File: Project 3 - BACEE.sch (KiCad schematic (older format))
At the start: 12 parts

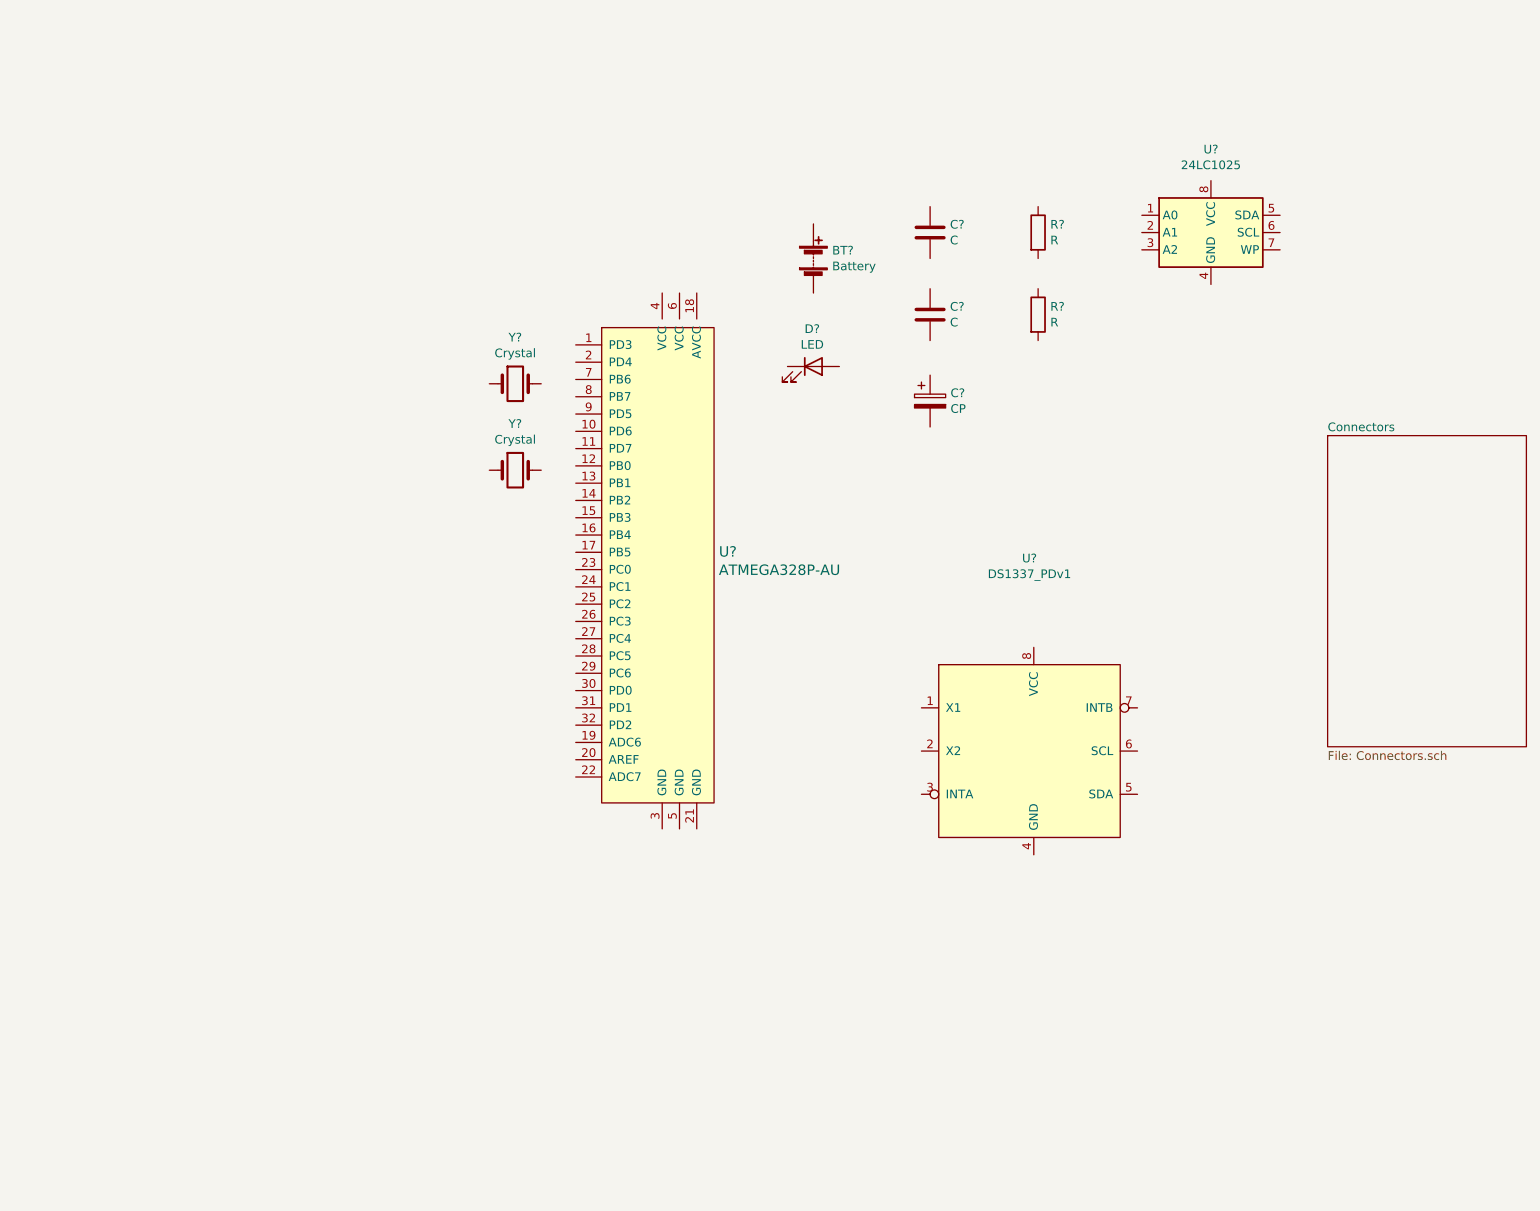
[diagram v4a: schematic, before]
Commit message: Arrenged symbols.
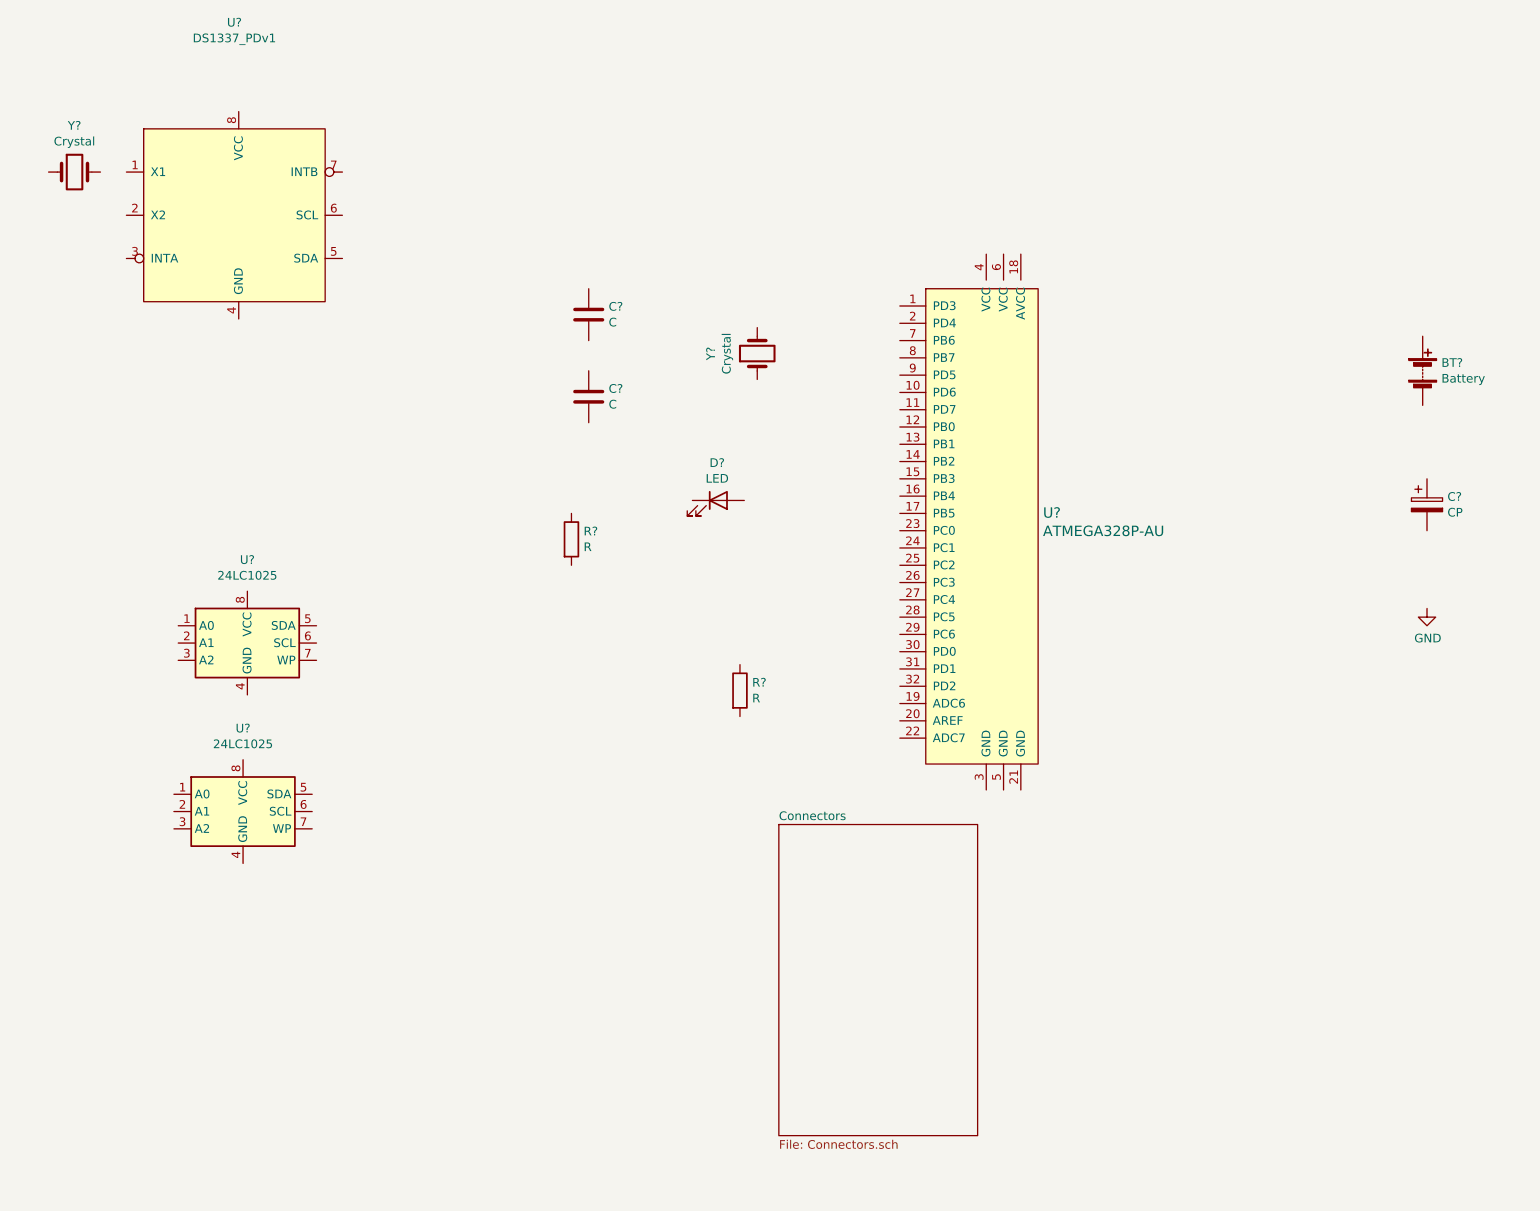
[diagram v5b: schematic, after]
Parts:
- added U?: 24LC1025, symbol Memory_EEPROM:24LC1025
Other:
- moved on the sheet: BT?, C?, D?, R?, U?, Y?
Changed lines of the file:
@@
 L Device:Battery BT?
 U 1 1 5F0CDB03
-P 5375 2275
-F 0 "BT?" H 5483 2321 50  0000 L CNN
-F 1 "Battery" H 5483 2230 50  0000 L CNN
-F 2 "" V 5375 2335 50  0001 C CNN
-F 3 "~" V 5375 2335 50  0001 C CNN
-	1    5375 2275
+P 8900 2925
+F 0 "BT?" H 9008 2971 50  0000 L CNN
+F 1 "Battery" H 9008 2880 50  0000 L CNN
+F 2 "" V 8900 2985 50  0001 C CNN
+F 3 "~" V 8900 2985 50  0001 C CNN
+	1    8900 2925
 	1    0    0    -1
 $EndComp
@@
 L Device:C C?
 U 1 1 5F0CEA38
-P 6050 2125
-F 0 "C?" H 6165 2171 50  0000 L CNN
-F 1 "C" H 6165 2080 50  0000 L CNN
-F 2 "" H 6088 1975 50  0001 C CNN
-F 3 "~" H 6050 2125 50  0001 C CNN
-	1    6050 2125
+P 4075 2600
+F 0 "C?" H 4190 2646 50  0000 L CNN
+F 1 "C" H 4190 2555 50  0000 L CNN
+F 2 "" H 4113 2450 50  0001 C CNN
+F 3 "~" H 4075 2600 50  0001 C CNN
+	1    4075 2600
 	1    0    0    -1
 $EndComp
@@
 L Device:C C?
 U 1 1 5F0CF2D4
-P 6050 2600
-F 0 "C?" H 6165 2646 50  0000 L CNN
-F 1 "C" H 6165 2555 50  0000 L CNN
-F 2 "" H 6088 2450 50  0001 C CNN
-F 3 "~" H 6050 2600 50  0001 C CNN
-	1    6050 2600
+P 4075 3075
+F 0 "C?" H 4190 3121 50  0000 L CNN
+F 1 "C" H 4190 3030 50  0000 L CNN
+F 2 "" H 4113 2925 50  0001 C CNN
+F 3 "~" H 4075 3075 50  0001 C CNN
+	1    4075 3075
 	1    0    0    -1
 $EndComp
@@
 L Device:CP C?
 U 1 1 5F0CF8DC
-P 6050 3100
-F 0 "C?" H 6168 3146 50  0000 L CNN
-F 1 "CP" H 6168 3055 50  0000 L CNN
-F 2 "" H 6088 2950 50  0001 C CNN
-F 3 "~" H 6050 3100 50  0001 C CNN
-	1    6050 3100
+P 8925 3700
+F 0 "C?" H 9043 3746 50  0000 L CNN
+F 1 "CP" H 9043 3655 50  0000 L CNN
+F 2 "" H 8963 3550 50  0001 C CNN
+F 3 "~" H 8925 3700 50  0001 C CNN
+	1    8925 3700
 	1    0    0    -1
 $EndComp
@@
 L Device:LED D?
 U 1 1 5F0CFE76
-P 5375 2900
-F 0 "D?" H 5368 3117 50  0000 C CNN
-F 1 "LED" H 5368 3026 50  0000 C CNN
-F 2 "" H 5375 2900 50  0001 C CNN
-F 3 "~" H 5375 2900 50  0001 C CNN
-	1    5375 2900
+P 4825 3675
+F 0 "D?" H 4818 3892 50  0000 C CNN
+F 1 "LED" H 4818 3801 50  0000 C CNN
+F 2 "" H 4825 3675 50  0001 C CNN
+F 3 "~" H 4825 3675 50  0001 C CNN
+	1    4825 3675
 	1    0    0    -1
 $EndComp
@@
 L Device:R R?
 U 1 1 5F0D09EF
-P 6675 2125
-F 0 "R?" H 6745 2171 50  0000 L CNN
-F 1 "R" H 6745 2080 50  0000 L CNN
-F 2 "" V 6605 2125 50  0001 C CNN
-F 3 "~" H 6675 2125 50  0001 C CNN
-	1    6675 2125
+P 3975 3900
+F 0 "R?" H 4045 3946 50  0000 L CNN
+F 1 "R" H 4045 3855 50  0000 L CNN
+F 2 "" V 3905 3900 50  0001 C CNN
+F 3 "~" H 3975 3900 50  0001 C CNN
+	1    3975 3900
 	1    0    0    -1
 $EndComp
@@
 L Device:R R?
 U 1 1 5F0D11B8
-P 6675 2600
-F 0 "R?" H 6745 2646 50  0000 L CNN
-F 1 "R" H 6745 2555 50  0000 L CNN
-F 2 "" V 6605 2600 50  0001 C CNN
-F 3 "~" H 6675 2600 50  0001 C CNN
-	1    6675 2600
+P 4950 4775
+F 0 "R?" H 5020 4821 50  0000 L CNN
+F 1 "R" H 5020 4730 50  0000 L CNN
+F 2 "" V 4880 4775 50  0001 C CNN
+F 3 "~" H 4950 4775 50  0001 C CNN
+	1    4950 4775
 	1    0    0    -1
 $EndComp
@@
 L Memory_EEPROM:24LC1025 U?
 U 1 1 5F0D1B59
-P 7675 2125
-F 0 "U?" H 7675 2606 50  0000 C CNN
-F 1 "24LC1025" H 7675 2515 50  0000 C CNN
-F 2 "" H 7675 2125 50  0001 C CNN
-F 3 "http://ww1.microchip.com/downloads/en/DeviceDoc/21941B.pdf" H 7675 2125 50  0001 C CNN
-	1    7675 2125
+P 2100 4500
+F 0 "U?" H 2100 4981 50  0000 C CNN
+F 1 "24LC1025" H 2100 4890 50  0000 C CNN
+F 2 "" H 2100 4500 50  0001 C CNN
+F 3 "http://ww1.microchip.com/downloads/en/DeviceDoc/21941B.pdf" H 2100 4500 50  0001 C CNN
+	1    2100 4500
 	1    0    0    -1
 $EndComp
 $Sheet
-S 8350 3300 1150 1800
+S 5175 5550 1150 1800
 U 5F0D3531
 F0 "Connectors" 50
@@
 L dk_Embedded-Microcontrollers:ATMEGA328P-AU U?
 U 1 1 5F0D825C
-P 4500 4075
-F 0 "U?" H 4828 4178 60  0000 L CNN
-F 1 "ATMEGA328P-AU" H 4828 4072 60  0000 L CNN
-F 2 "digikey-footprints:TQFP-32_7x7mm" H 4700 4275 60  0001 L CNN
-F 3 "http://www.microchip.com/mymicrochip/filehandler.aspx?ddocname=en608326" H 4700 4375 60  0001 L CNN
-F 4 "ATMEGA328P-AU-ND" H 4700 4475 60  0001 L CNN "Digi-Key_PN"
-F 5 "ATMEGA328P-AU" H 4700 4575 60  0001 L CNN "MPN"
-F 6 "Integrated Circuits (ICs)" H 4700 4675 60  0001 L CNN "Category"
-F 7 "Embedded - Microcontrollers" H 4700 4775 60  0001 L CNN "Family"
-F 8 "http://www.microchip.com/mymicrochip/filehandler.aspx?ddocname=en608326" H 4700 4875 60  0001 L CNN "DK_Datasheet_Link"
-F 9 "/product-detail/en/microchip-technology/ATMEGA328P-AU/ATMEGA328P-AU-ND/1832260" H 4700 4975 60  0001 L CNN "DK_Detail_Page"
-F 10 "IC MCU 8BIT 32KB FLASH 32TQFP" H 4700 5075 60  0001 L CNN "Description"
-F 11 "Microchip Technology" H 4700 5175 60  0001 L CNN "Manufacturer"
-F 12 "Active" H 4700 5275 60  0001 L CNN "Status"
-	1    4500 4075
+P 6375 3850
+F 0 "U?" H 6703 3953 60  0000 L CNN
+F 1 "ATMEGA328P-AU" H 6703 3847 60  0000 L CNN
+F 2 "digikey-footprints:TQFP-32_7x7mm" H 6575 4050 60  0001 L CNN
+F 3 "http://www.microchip.com/mymicrochip/filehandler.aspx?ddocname=en608326" H 6575 4150 60  0001 L CNN
+F 4 "ATMEGA328P-AU-ND" H 6575 4250 60  0001 L CNN "Digi-Key_PN"
+F 5 "ATMEGA328P-AU" H 6575 4350 60  0001 L CNN "MPN"
+F 6 "Integrated Circuits (ICs)" H 6575 4450 60  0001 L CNN "Category"
+F 7 "Embedded - Microcontrollers" H 6575 4550 60  0001 L CNN "Family"
+F 8 "http://www.microchip.com/mymicrochip/filehandler.aspx?ddocname=en608326" H 6575 4650 60  0001 L CNN "DK_Datasheet_Link"
+F 9 "/product-detail/en/microchip-technology/ATMEGA328P-AU/ATMEGA328P-AU-ND/1832260" H 6575 4750 60  0001 L CNN "DK_Detail_Page"
+F 10 "IC MCU 8BIT 32KB FLASH 32TQFP" H 6575 4850 60  0001 L CNN "Description"
+F 11 "Microchip Technology" H 6575 4950 60  0001 L CNN "Manufacturer"
+F 12 "Active" H 6575 5050 60  0001 L CNN "Status"
+	1    6375 3850
 	1    0    0    -1
 $EndComp
@@
 L Project3:DS1337_PDv1 U?
 U 1 1 5F0DBCFF
-P 6650 5125
-F 0 "U?" H 6625 6240 50  0000 C CNN
-F 1 "DS1337_PDv1" H 6625 6149 50  0000 C CNN
-F 2 "" H 6350 5475 50  0001 C CNN
-F 3 "https://datasheets.maximintegrated.com/en/ds/DS1337-DS1337C.pdf" H 6350 5475 50  0001 C CNN
-	1    6650 5125
+P 2050 2025
+F 0 "U?" H 2025 3140 50  0000 C CNN
+F 1 "DS1337_PDv1" H 2025 3049 50  0000 C CNN
+F 2 "" H 1750 2375 50  0001 C CNN
+F 3 "https://datasheets.maximintegrated.com/en/ds/DS1337-DS1337C.pdf" H 1750 2375 50  0001 C CNN
+	1    2050 2025
 	1    0    0    -1
 $EndComp
@@
 L Device:Crystal Y?
 U 1 1 5F0E9423
-P 3650 3000
-F 0 "Y?" H 3650 3268 50  0000 C CNN
-F 1 "Crystal" H 3650 3177 50  0000 C CNN
-F 2 "" H 3650 3000 50  0001 C CNN
-F 3 "~" H 3650 3000 50  0001 C CNN
-	1    3650 3000
+P 1100 1775
+F 0 "Y?" H 1100 2043 50  0000 C CNN
+F 1 "Crystal" H 1100 1952 50  0000 C CNN
+F 2 "" H 1100 1775 50  0001 C CNN
+F 3 "~" H 1100 1775 50  0001 C CNN
+	1    1100 1775
 	1    0    0    -1
 $EndComp
@@
 L Device:Crystal Y?
 U 1 1 5F0EA205
-P 3650 3500
-F 0 "Y?" H 3650 3768 50  0000 C CNN
-F 1 "Crystal" H 3650 3677 50  0000 C CNN
-F 2 "" H 3650 3500 50  0001 C CNN
-F 3 "~" H 3650 3500 50  0001 C CNN
-	1    3650 3500
+P 5050 2825
+F 0 "Y?" H 5050 3093 50  0000 C CNN
+F 1 "Crystal" H 5050 3002 50  0000 C CNN
+F 2 "" H 5050 2825 50  0001 C CNN
+F 3 "~" H 5050 2825 50  0001 C CNN
+	1    5050 2825
+	0    -1   -1   0
+$EndComp
+$Comp
+L Memory_EEPROM:24LC1025 U?
+U 1 1 5F0EDBCB
+P 2075 5475
+F 0 "U?" H 2075 5956 50  0000 C CNN
+F 1 "24LC1025" H 2075 5865 50  0000 C CNN
+F 2 "" H 2075 5475 50  0001 C CNN
+F 3 "http://ww1.microchip.com/downloads/en/DeviceDoc/21941B.pdf" H 2075 5475 50  0001 C CNN
+	1    2075 5475
 	1    0    0    -1
 $EndComp
+$Comp
+L power:GND #PWR?
+U 1 1 5F0FD4A6
+P 8925 4300
+F 0 "#PWR?" H 8925 4050 50  0001 C CNN
+F 1 "GND" H 8930 4127 50  0000 C CNN
+F 2 "" H 8925 4300 50  0001 C CNN
+F 3 "" H 8925 4300 50  0001 C CNN
+	1    8925 4300
+	1    0    0    -1
+$EndComp

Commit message: Annotated.
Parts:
- gave numbers to parts that had none: 13
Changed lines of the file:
@@
 $EndDescr
 $Comp
-L Device:Battery BT?
+L Device:Battery BT1
 U 1 1 5F0CDB03
 P 8900 2925
-F 0 "BT?" H 9008 2971 50  0000 L CNN
+F 0 "BT1" H 9008 2971 50  0000 L CNN
 F 1 "Battery" H 9008 2880 50  0000 L CNN
 F 2 "" V 8900 2985 50  0001 C CNN
@@
 $EndComp
 $Comp
-L Device:C C?
+L Device:C C1
 U 1 1 5F0CEA38
 P 4075 2600
-F 0 "C?" H 4190 2646 50  0000 L CNN
+F 0 "C1" H 4190 2646 50  0000 L CNN
 F 1 "C" H 4190 2555 50  0000 L CNN
 F 2 "" H 4113 2450 50  0001 C CNN
@@
 $EndComp
 $Comp
-L Device:C C?
+L Device:C C2
 U 1 1 5F0CF2D4
 P 4075 3075
-F 0 "C?" H 4190 3121 50  0000 L CNN
+F 0 "C2" H 4190 3121 50  0000 L CNN
 F 1 "C" H 4190 3030 50  0000 L CNN
 F 2 "" H 4113 2925 50  0001 C CNN
@@
 $EndComp
 $Comp
-L Device:CP C?
+L Device:CP C3
 U 1 1 5F0CF8DC
 P 8925 3700
-F 0 "C?" H 9043 3746 50  0000 L CNN
+F 0 "C3" H 9043 3746 50  0000 L CNN
 F 1 "CP" H 9043 3655 50  0000 L CNN
 F 2 "" H 8963 3550 50  0001 C CNN
@@
 $EndComp
 $Comp
-L Device:LED D?
+L Device:LED D1
 U 1 1 5F0CFE76
 P 4825 3675
-F 0 "D?" H 4818 3892 50  0000 C CNN
+F 0 "D1" H 4818 3892 50  0000 C CNN
 F 1 "LED" H 4818 3801 50  0000 C CNN
 F 2 "" H 4825 3675 50  0001 C CNN
@@
 $EndComp
 $Comp
-L Device:R R?
+L Device:R R1
 U 1 1 5F0D09EF
 P 3975 3900
-F 0 "R?" H 4045 3946 50  0000 L CNN
+F 0 "R1" H 4045 3946 50  0000 L CNN
 F 1 "R" H 4045 3855 50  0000 L CNN
 F 2 "" V 3905 3900 50  0001 C CNN
@@
 $EndComp
 $Comp
-L Device:R R?
+L Device:R R2
 U 1 1 5F0D11B8
 P 4950 4775
-F 0 "R?" H 5020 4821 50  0000 L CNN
+F 0 "R2" H 5020 4821 50  0000 L CNN
 F 1 "R" H 5020 4730 50  0000 L CNN
 F 2 "" V 4880 4775 50  0001 C CNN
@@
 $EndComp
 $Comp
-L Memory_EEPROM:24LC1025 U?
+L Memory_EEPROM:24LC1025 U3
 U 1 1 5F0D1B59
 P 2100 4500
-F 0 "U?" H 2100 4981 50  0000 C CNN
+F 0 "U3" H 2100 4981 50  0000 C CNN
 F 1 "24LC1025" H 2100 4890 50  0000 C CNN
 F 2 "" H 2100 4500 50  0001 C CNN
@@
 $EndSheet
 $Comp
-L dk_Embedded-Microcontrollers:ATMEGA328P-AU U?
+L dk_Embedded-Microcontrollers:ATMEGA328P-AU U4
 U 1 1 5F0D825C
 P 6375 3850
-F 0 "U?" H 6703 3953 60  0000 L CNN
+F 0 "U4" H 6703 3953 60  0000 L CNN
 F 1 "ATMEGA328P-AU" H 6703 3847 60  0000 L CNN
 F 2 "digikey-footprints:TQFP-32_7x7mm" H 6575 4050 60  0001 L CNN
@@
 $EndComp
 $Comp
-L Project3:DS1337_PDv1 U?
+L Project3:DS1337_PDv1 U1
 U 1 1 5F0DBCFF
 P 2050 2025
-F 0 "U?" H 2025 3140 50  0000 C CNN
+F 0 "U1" H 2025 3140 50  0000 C CNN
 F 1 "DS1337_PDv1" H 2025 3049 50  0000 C CNN
 F 2 "" H 1750 2375 50  0001 C CNN
@@
 $EndComp
 $Comp
-L Device:Crystal Y?
+L Device:Crystal Y1
 U 1 1 5F0E9423
 P 1100 1775
-F 0 "Y?" H 1100 2043 50  0000 C CNN
+F 0 "Y1" H 1100 2043 50  0000 C CNN
 F 1 "Crystal" H 1100 1952 50  0000 C CNN
 F 2 "" H 1100 1775 50  0001 C CNN
@@
 $EndComp
 $Comp
-L Device:Crystal Y?
+L Device:Crystal Y2
 U 1 1 5F0EA205
 P 5050 2825
-F 0 "Y?" H 5050 3093 50  0000 C CNN
+F 0 "Y2" H 5050 3093 50  0000 C CNN
 F 1 "Crystal" H 5050 3002 50  0000 C CNN
 F 2 "" H 5050 2825 50  0001 C CNN
@@
 $EndComp
 $Comp
-L Memory_EEPROM:24LC1025 U?
+L Memory_EEPROM:24LC1025 U2
 U 1 1 5F0EDBCB
 P 2075 5475
-F 0 "U?" H 2075 5956 50  0000 C CNN
+F 0 "U2" H 2075 5956 50  0000 C CNN
 F 1 "24LC1025" H 2075 5865 50  0000 C CNN
 F 2 "" H 2075 5475 50  0001 C CNN
@@
 $EndComp
 $Comp
-L power:GND #PWR?
+L power:GND #PWR01
 U 1 1 5F0FD4A6
 P 8925 4300
-F 0 "#PWR?" H 8925 4050 50  0001 C CNN
+F 0 "#PWR01" H 8925 4050 50  0001 C CNN
 F 1 "GND" H 8930 4127 50  0000 C CNN
 F 2 "" H 8925 4300 50  0001 C CNN
